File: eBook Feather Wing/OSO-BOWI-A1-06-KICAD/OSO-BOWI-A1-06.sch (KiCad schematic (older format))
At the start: 101 parts, among them IC1 MCP23008_SO, IC2 23K256-I/SN, IC3 MICROBUILDER_SPIFLASH_SOIC8, J1 SJ-43514-SMT, Q1 IRLML0100, SW1 SPDT_SWITCH

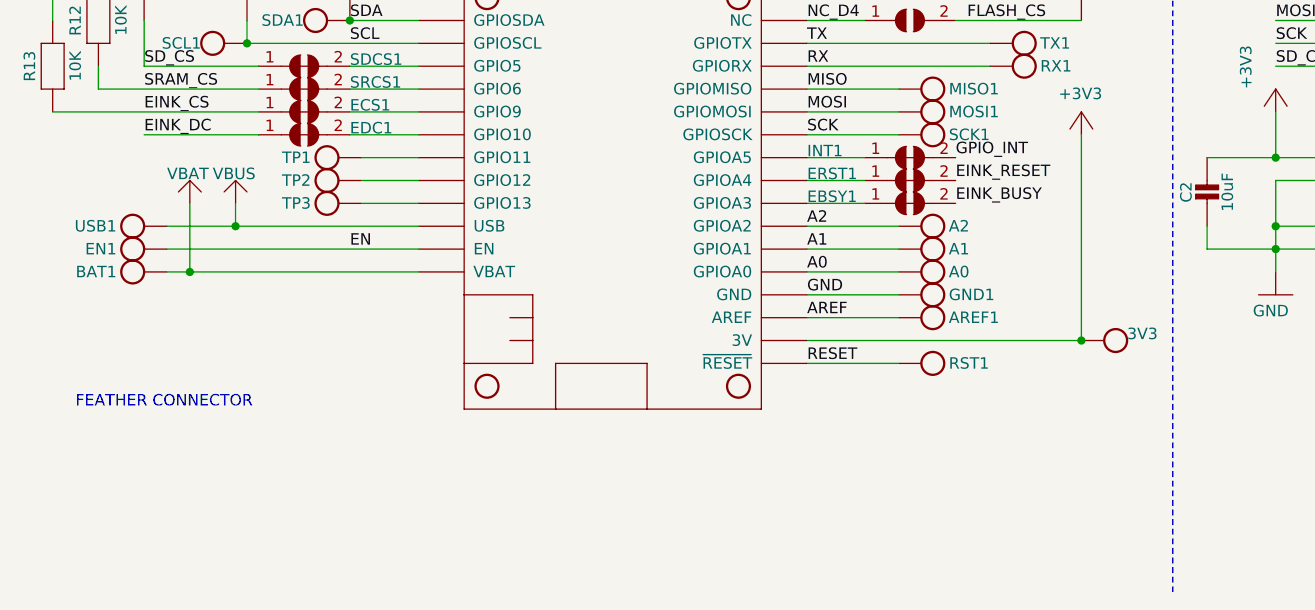
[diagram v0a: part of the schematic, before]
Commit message: Revised E-Book Wing silkscreen labels.
Addressing comment for the solder jumpers on the E-Book Wing that had silkscreen labels, such as TX1/RX1/ECS1 etc, where the number 1 was appended after the original name, which was crowding the labels and making the text less readable. The affected files are updated.
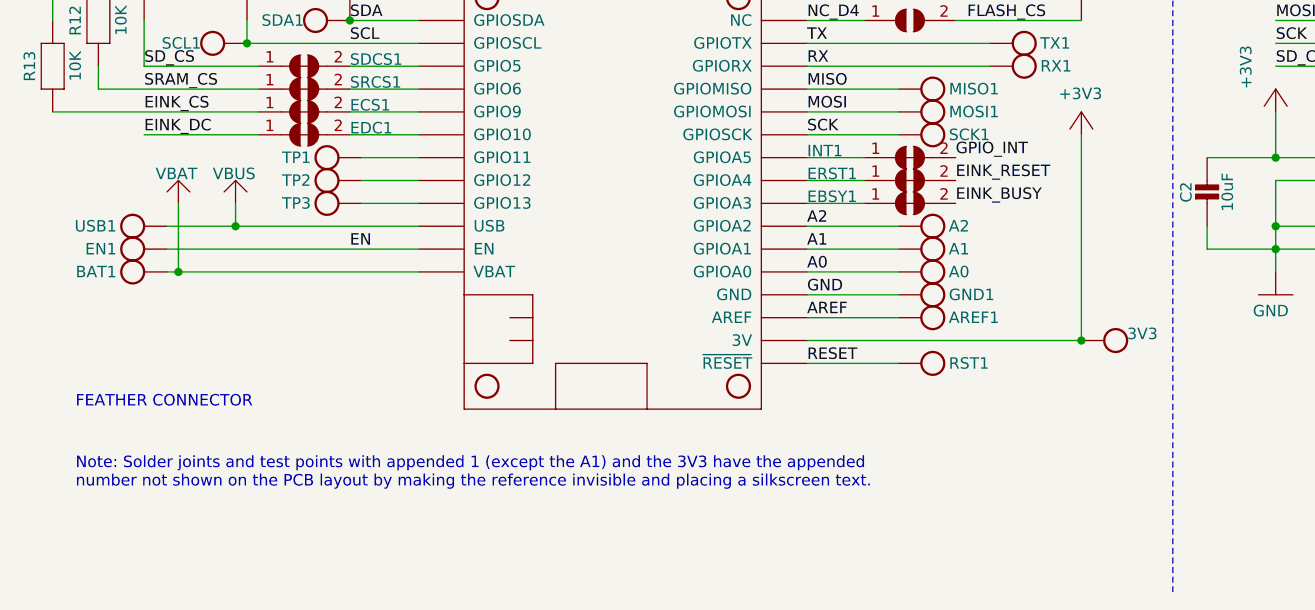
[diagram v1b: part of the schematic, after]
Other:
- note added: "Note: Solder joints and test points with appended 1 (except the A1) and the 3V3 have the appended\nnumber not shown on the PCB layout by making the reference invisible and placing a silkscreen text."
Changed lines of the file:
@@
 SDA
 Wire Wire Line
-	1250 6300 1250 6600
-Wire Wire Line
-	2250 6600 1250 6600
-Wire Wire Line
-	1250 6600 1150 6600
-Connection ~ 1250 6600
+	1200 6300 1200 6600
+Wire Wire Line
+	2250 6600 1200 6600
+Wire Wire Line
+	1200 6600 1150 6600
+Connection ~ 1200 6600
 Wire Wire Line
 	2250 6500 1150 6500
@@
 L OSO-BOWI-A1-06-eagle-import:VBAT #U$022
 U 1 0 3E45157DD872CB34
-P 1250 6200
-F 0 "#U$022" H 1250 6200 50  0001 C CNN
-F 1 "VBAT" H 1150 6200 50  0000 L BNN
-F 2 "" H 1250 6200 50  0001 C CNN
-F 3 "" H 1250 6200 50  0001 C CNN
-	1    1250 6200
+P 1200 6200
+F 0 "#U$022" H 1200 6200 50  0001 C CNN
+F 1 "VBAT" H 1100 6200 50  0000 L BNN
+F 2 "" H 1200 6200 50  0001 C CNN
+F 3 "" H 1200 6200 50  0001 C CNN
+	1    1200 6200
 	1    0    0    -1
 $EndComp
@@
 Wire Wire Line
 	8650 4300 8850 4300
+Text Notes 750  7550 0    50   ~ 0
+Note: Solder joints and test points with appended 1 (except the A1) and the 3V3 have the appended\nnumber not shown on the PCB layout by making the reference invisible and placing a silkscreen text.
 $EndSCHEMATC
